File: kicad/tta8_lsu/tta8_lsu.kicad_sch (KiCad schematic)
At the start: 15 parts, among them J1 Conn_02x32_Counter_Clockwise, J2 Conn_01x06, J3 Conn_02x02_Odd_Even, U1 74AHCT573, U2 74AHCT573, U3 74AHCT573, U4 74AHCT573, U5 74AHCT573, U6 74AHCT573, U7 74AHCT00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

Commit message: Fix second address pointer register
Was T->A supposed to be T->T
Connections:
- net A0: no longer U4.12 (Q7)
- net A1: no longer U4.13 (Q6)
- net A10: no longer U3.14 (Q5)
- net A11: no longer U3.15 (Q4)
- net A12: no longer U3.16 (Q3)
- net A13: no longer U3.17 (Q2)
- net A14: no longer U3.18 (Q1)
- net A15: no longer U3.19 (Q0)
- net A2: no longer U4.14 (Q5)
- net A3: no longer U4.15 (Q4)
- net A4: no longer U4.16 (Q3)
- net A5: no longer U4.17 (Q2)
- net A6: no longer U4.18 (Q1)
- net A7: no longer U4.19 (Q0)
- net A8: no longer U3.12 (Q7)
- net A9: no longer U3.13 (Q6)
- net T0: now also U4.12 (Q7)
- net T1: now also U4.13 (Q6)
- net T10: now also U3.14 (Q5)
- net T11: now also U3.15 (Q4)
- net T12: now also U3.16 (Q3)
- net T13: now also U3.17 (Q2)
- net T14: now also U3.18 (Q1)
- net T15: now also U3.19 (Q0)
- net T2: now also U4.14 (Q5)
- net T3: now also U4.15 (Q4)
- net T4: now also U4.16 (Q3)
- net T5: now also U4.17 (Q2)
- net T6: now also U4.18 (Q1)
- net T7: now also U4.19 (Q0)
- net T8: now also U3.12 (Q7)
- net T9: now also U3.13 (Q6)
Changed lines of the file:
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@@
 		)
 	)
-	(label "A0"
+	(label "T0"
 		(at 100.33 109.22 0)
 		(effects
@@
 		)
 	)
-	(label "A2"
+	(label "T2"
 		(at 100.33 104.14 0)
 		(effects
@@
 		)
 	)
-	(label "A13"
+	(label "T13"
 		(at 100.33 43.18 0)
 		(effects
@@
 		)
 	)
-	(label "A7"
+	(label "T7"
 		(at 100.33 91.44 0)
 		(effects
@@
 		)
 	)
-	(label "A14"
+	(label "T14"
 		(at 100.33 40.64 0)
 		(effects
@@
 		)
 	)
-	(label "A9"
+	(label "T9"
 		(at 100.33 53.34 0)
 		(effects
@@
 		)
 	)
-	(label "A11"
+	(label "T11"
 		(at 100.33 48.26 0)
 		(effects
@@
 		)
 	)
-	(label "A4"
+	(label "T4"
 		(at 100.33 99.06 0)
 		(effects
@@
 		)
 	)
-	(label "A6"
+	(label "T6"
 		(at 100.33 93.98 0)
 		(effects
@@
 		)
 	)
-	(label "A8"
+	(label "T8"
 		(at 100.33 55.88 0)
 		(effects
@@
 		)
 	)
-	(label "A12"
+	(label "T12"
 		(at 100.33 45.72 0)
 		(effects
@@
 		)
 	)
-	(label "A3"
+	(label "T3"
 		(at 100.33 101.6 0)
 		(effects
@@
 		)
 	)
-	(label "A5"
+	(label "T5"
 		(at 100.33 96.52 0)
 		(effects
@@
 		)
 	)
-	(label "A10"
+	(label "T10"
 		(at 100.33 50.8 0)
 		(effects
@@
 		)
 	)
-	(label "A1"
+	(label "T1"
 		(at 100.33 106.68 0)
 		(effects
@@
 		)
 	)
-	(label "A15"
+	(label "T15"
 		(at 100.33 38.1 0)
 		(effects

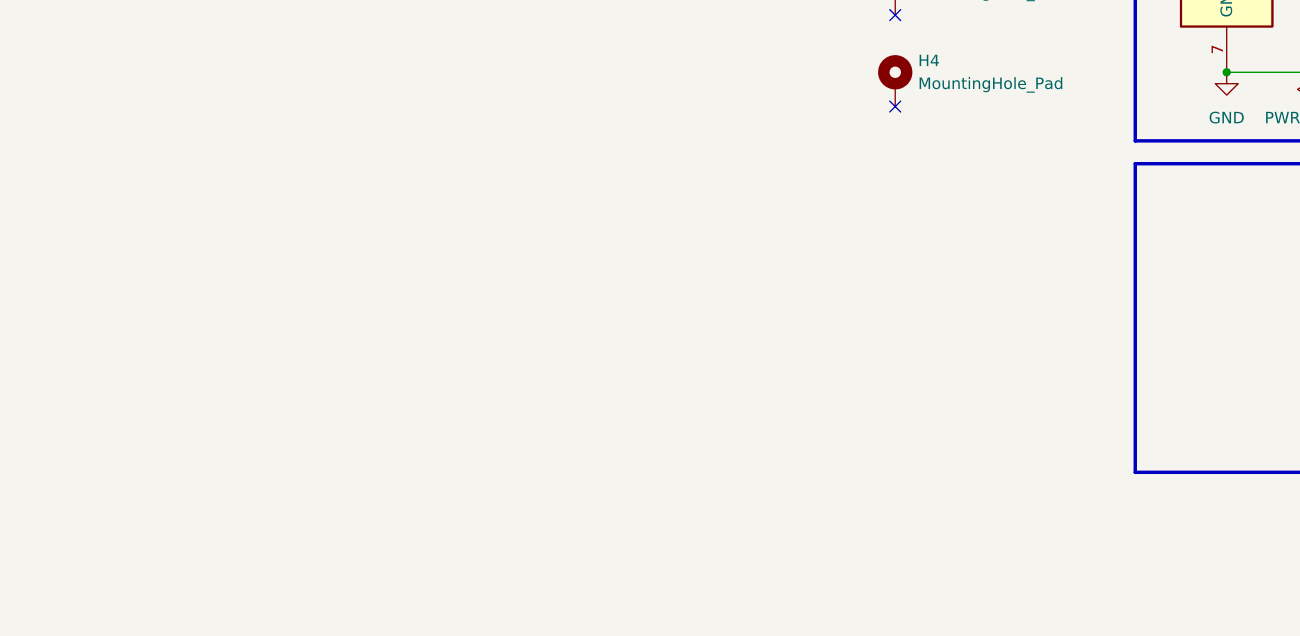
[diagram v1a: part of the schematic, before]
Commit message: Add decoupling to tt8 lsu
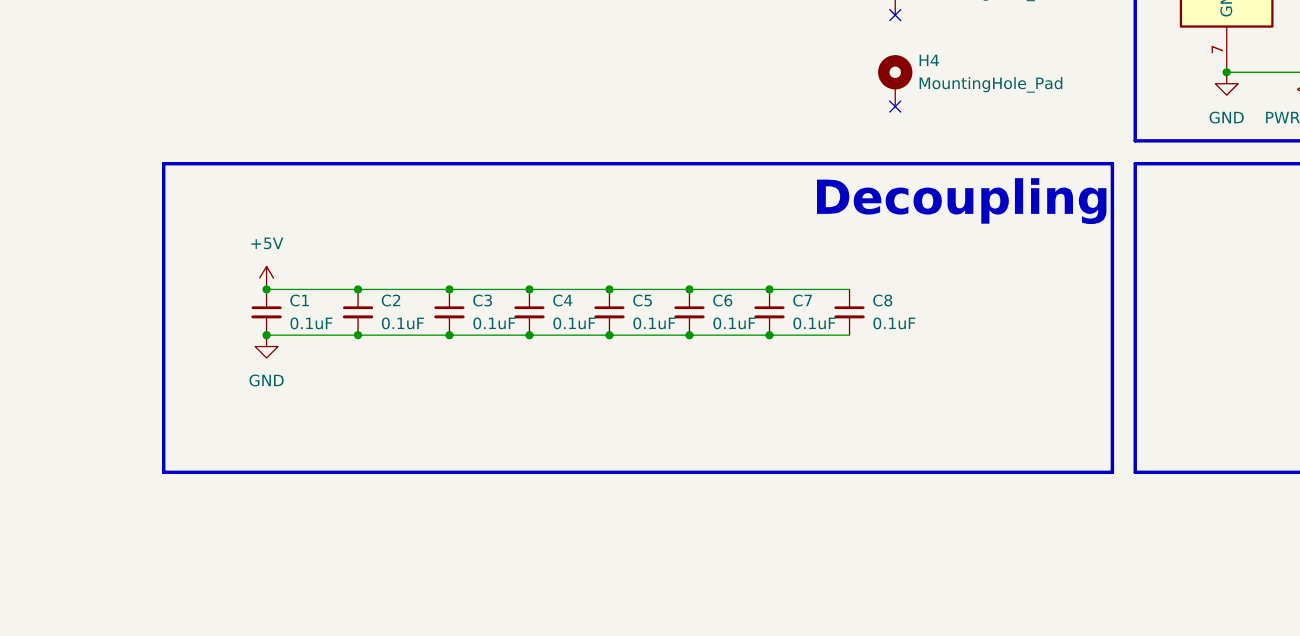
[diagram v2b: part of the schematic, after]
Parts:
- added C1, C2, C3, C4, C5, C6, C7, C8: 0.1uF, Capacitor_THT:C_Disc_D5.0mm_W2.5mm_P2.50mm, symbol Device:C_Small
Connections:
- net +5V: now also C1.1, C2.1, C3.1, C4.1, C5.1, C6.1, C7.1, C8.1
- net GND: now also C1.2, C2.2, C3.2, C4.2, C5.2, C6.2, C7.2, C8.2
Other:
- note added: "Decoupling"
